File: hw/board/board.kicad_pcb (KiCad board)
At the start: 4 copper layers, 100 x 85 mm, 60 parts, among them U1 XC7A35T-FTG256, U2 TPS54331DR, U3 AP7361C-18SP-13, U4 AP7361C-10E, U5 STM32F302CBTx, U6 W25Q128JVSIQTR

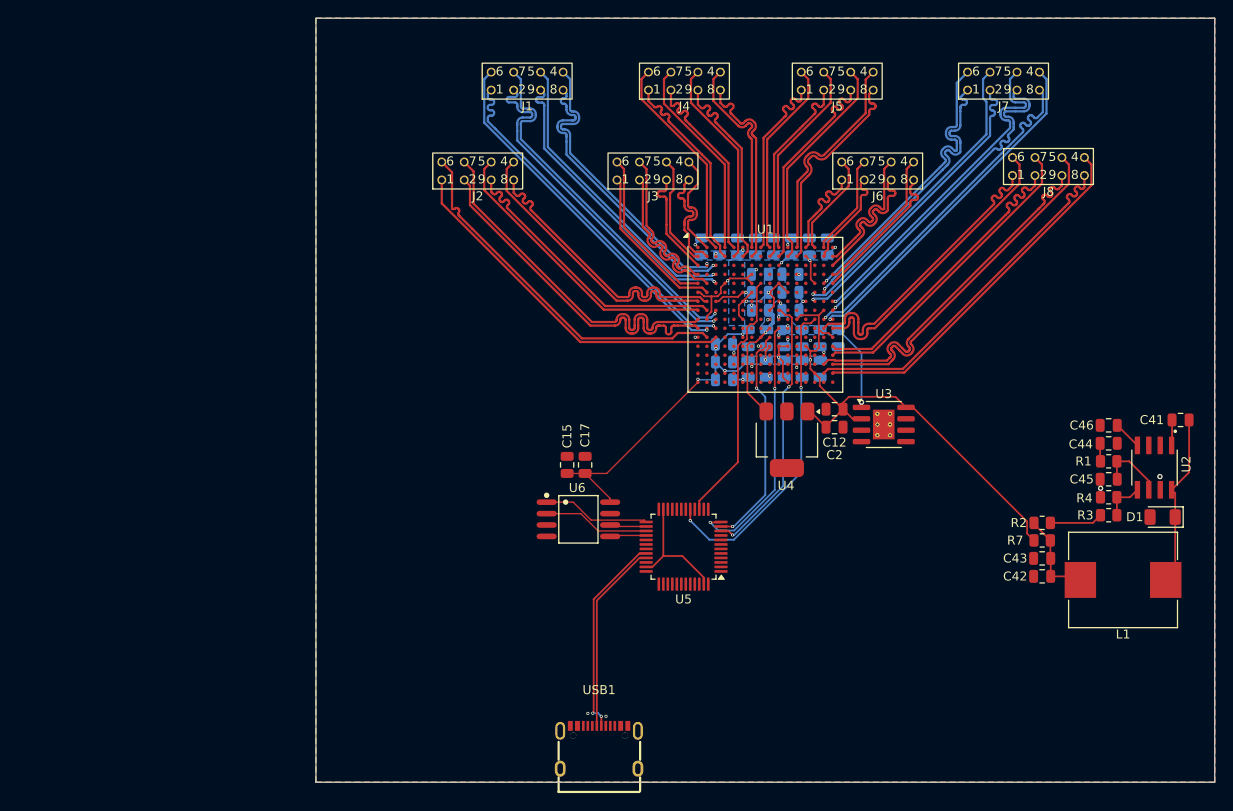
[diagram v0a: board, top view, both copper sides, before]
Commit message: Began refactoring BGA fanout
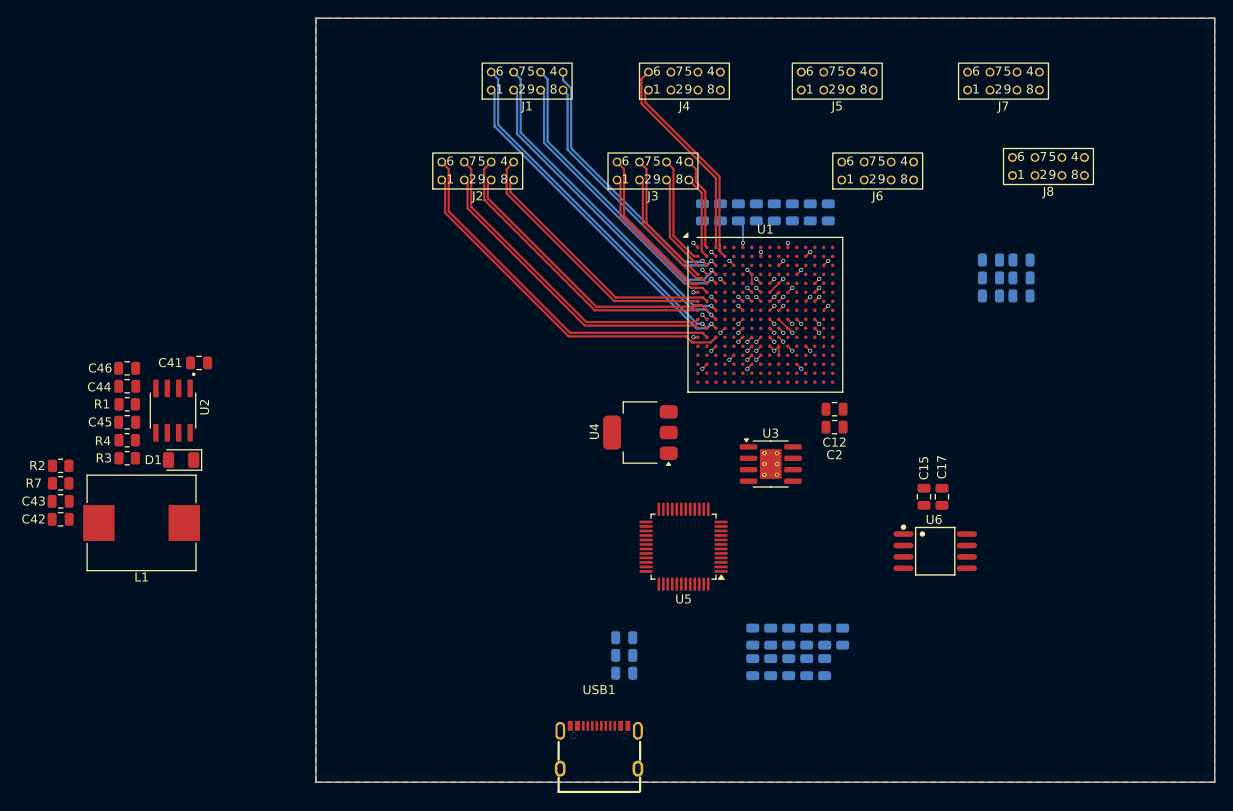
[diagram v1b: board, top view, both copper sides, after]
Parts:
- moved C44 109.4 mm to (63.0, 81.0)
- moved C45 109.4 mm to (63.0, 85.0)
- moved C42 109.4 mm to (55.6, 95.8)
- moved C43 109.4 mm to (55.6, 93.8)
- moved L1 109.4 mm to (64.6, 96.2)
- moved R2 109.4 mm to (55.6, 89.8)
- moved R7 109.4 mm to (55.6, 91.8)
- moved U2 109.4 mm to (68.1, 83.7)
- moved C41 109.4 mm to (71.0, 78.4)
- moved C46 109.4 mm to (63.0, 79.0)
- moved R1 109.4 mm to (63.0, 83.0)
- moved R3 109.4 mm to (63.0, 89.0)
- moved R4 109.4 mm to (63.0, 87.0)
- moved D1 109.4 mm to (69.0, 89.2)
- moved C15 39.9 mm to (151.7, 93.2)
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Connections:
- net VCCO_14 renamed +2V5
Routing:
- net +2V5: track 122.8 -> 17.0 mm, vias 14 -> 17
- net S_{out}8_N: track 40.9 -> 0.00 mm
- net S_{out}8_P: track 40.8 -> 0.00 mm
- net D_{out}8_N: track 40.7 -> 0.00 mm
- net D_{out}8_P: track 40.7 -> 0.00 mm
- net S_{out}7_N: track 38.9 -> 0.00 mm, vias 1 -> 0
- net S_{out}7_P: track 38.8 -> 0.00 mm, vias 1 -> 0
- net D_{out}7_N: track 38.8 -> 0.00 mm, vias 1 -> 0
- net D_{out}7_P: track 38.7 -> 0.00 mm, vias 1 -> 0
- net DIN: track 35.7 -> 0.71 mm, vias 2 -> 1
- net S_{in}8_N: track 34.4 -> 0.00 mm
- net D_{in}8_N: track 34.3 -> 0.00 mm
- net S_{in}8_P: track 34.3 -> 0.00 mm
- net D_{in}8_P: track 34.2 -> 0.00 mm
- net S_{in}7_N: track 34.4 -> 0.71 mm
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- removed copper zone on B.Cu, net +1V0
- removed copper zone on B.Cu, net +1V8
- removed copper zone on B.Cu, net +2V5

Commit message: Finished re-routing spacewire connectors
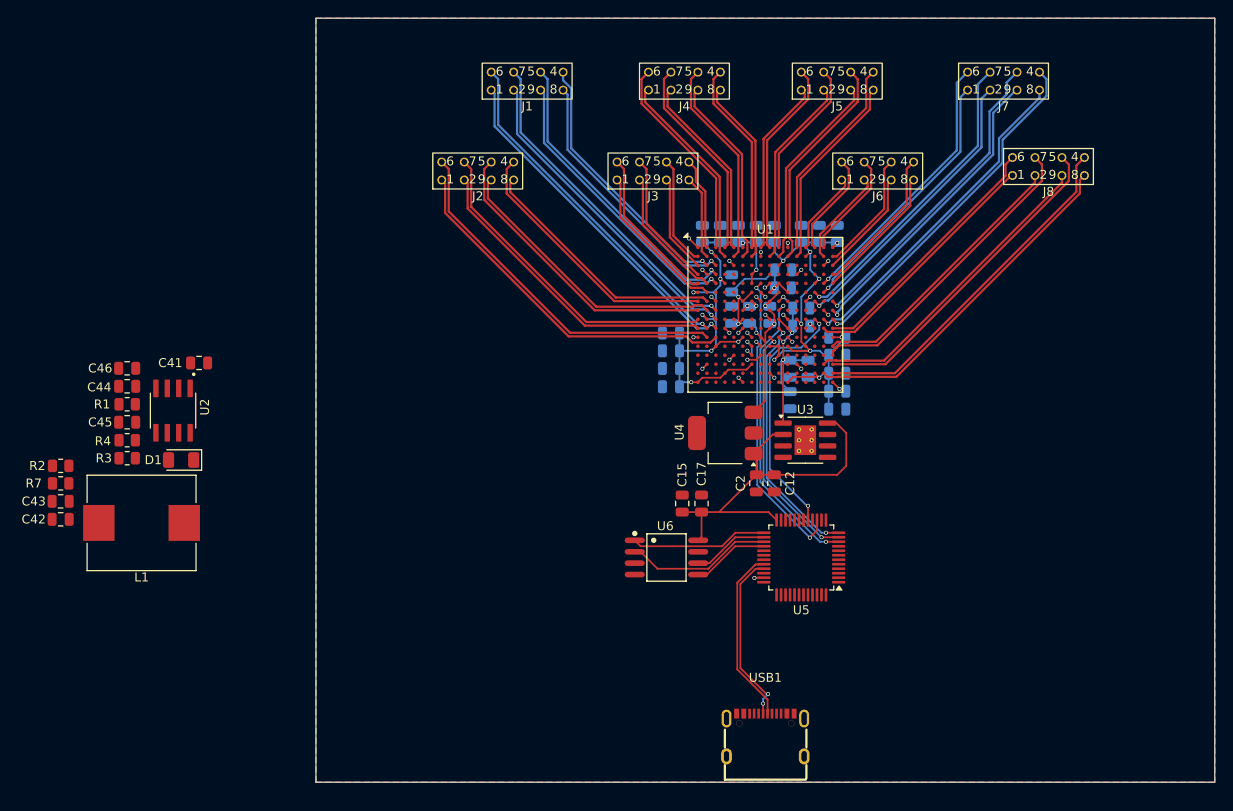
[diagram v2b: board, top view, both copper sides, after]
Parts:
- moved C8 40.8 mm to (136.0, 68.0), turned to 0 degrees
- moved C33 34.7 mm to (142.0, 77.5), turned to 0 degrees
- moved C16 34.6 mm to (142.0, 75.5), turned to 180 degrees
- moved C4 34.6 mm to (138.0, 74.2), turned to 0 degrees
- moved C35 34.3 mm to (123.5, 79.0)
- moved C37 34.3 mm to (123.5, 77.0)
- moved C36 34.3 mm to (123.5, 75.0)
- moved C32 32.9 mm to (142.0, 79.5), turned to 0 degrees
- moved C1 32.5 mm to (123.5, 81.0), turned to 180 degrees
- moved C14 32.4 mm to (130.2, 69.5), turned to 90 degrees
- moved C34 31.2 mm to (142.0, 81.5), turned to 0 degrees
- moved C9 30.0 mm to (136.8, 79.0)
- moved U6 29.9 mm to (123.0, 100.0)
- moved C3 29.9 mm to (138.8, 79.0)
- moved C31 29.6 mm to (142.0, 83.5), turned to 0 degrees
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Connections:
- U5 pad 1: unconnected-(U5-VBAT-Pad1) -> +2V5
- U5 pad 23: Net-(U5-VSS-Pad23) -> GND
- U5 pad 24: unconnected-(U5-VDD-Pad24) -> +2V5
- U5 pad 35: Net-(U5-VSS-Pad23) -> GND
- U5 pad 36: unconnected-(U5-VDD-Pad36) -> +2V5
- U5 pad 47: Net-(U5-VSS-Pad23) -> GND
- U5 pad 48: unconnected-(U5-VDD-Pad48) -> +2V5
- U5 pad 8: unconnected-(U5-VSSA-Pad8) -> GND
- U5 pad 9: unconnected-(U5-VDDA-Pad9) -> +2V5
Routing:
- net +2V5: track 17.0 -> 155.0 mm, vias 17 -> 19
- net S_{out}8_N: track 0.00 -> 39.6 mm
- net S_{out}8_P: track 0.00 -> 39.3 mm
- net S_{out}7_N: track 0.00 -> 39.0 mm, vias 0 -> 1
- net D_{out}8_N: track 0.00 -> 37.6 mm
- net S_{out}7_P: track 0.00 -> 37.0 mm, vias 0 -> 1
- net D_{out}8_P: track 0.00 -> 35.7 mm
- net D_{out}7_N: track 0.00 -> 35.0 mm, vias 0 -> 1
- net S_{in}8_N: track 0.00 -> 34.5 mm
- net D_{out}7_P: track 0.00 -> 34.1 mm, vias 0 -> 1
- net S_{in}7_N: track 0.71 -> 34.1 mm
- net CCLK: track 0.71 -> 33.6 mm, vias 1 -> 2
- net DONE: track 0.71 -> 32.8 mm, vias 1 -> 2
- net S_{in}7_P: track 0.71 -> 32.8 mm
- net S_{in}8_P: track 0.00 -> 30.8 mm
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
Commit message: Added reset + boot switches for STM32, re-routed power
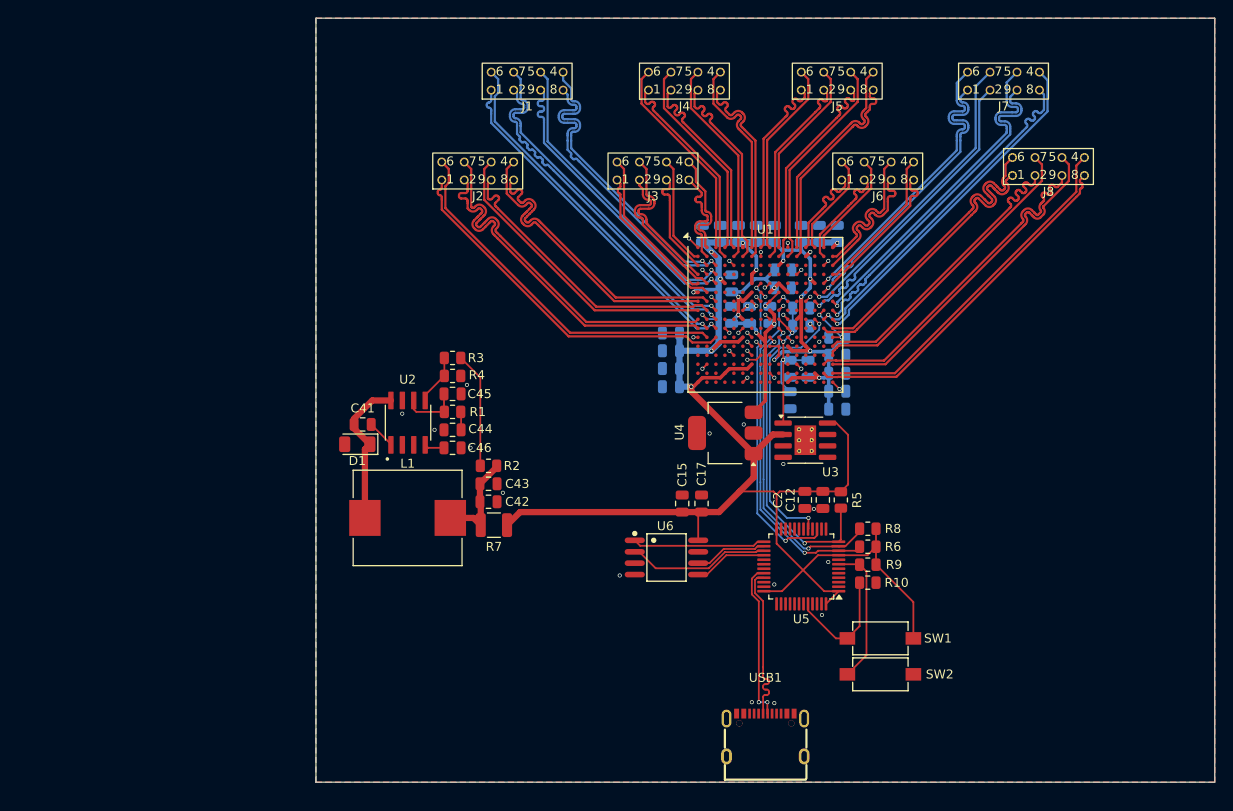
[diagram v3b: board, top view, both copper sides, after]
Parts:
- added R10: 4k7, Resistor_SMD:R_0805_2012Metric, F.Cu at (145.4, 102.8)
- added R5: 4k7, Resistor_SMD:R_0805_2012Metric, F.Cu at (142.4, 93.6)
- added R6: 330, Resistor_SMD:R_0805_2012Metric, F.Cu at (145.4, 98.8)
- added R8: 4k7, Resistor_SMD:R_0805_2012Metric, F.Cu at (145.4, 96.8)
- added R9: 4k7, Resistor_SMD:R_0805_2012Metric, F.Cu at (145.4, 100.8)
- added SW1: TSB008A2526A, EasyEDA:SW-SMD_L6.0-W3.5-LS8.0, F.Cu at (146.8, 109.0)
- added SW2: TSB008A2526A, EasyEDA:SW-SMD_L6.0-W3.5-LS8.0, F.Cu at (146.8, 113.0)
- R7: footprint Resistor_SMD:R_0805_2012Metric -> Resistor_SMD:R_1210_3225Metric
- moved R7 48.4 mm to (103.8, 96.4), turned to 0 degrees
- moved C43 47.6 mm to (103.2, 91.8), turned to 0 degrees
- moved C42 47.6 mm to (103.2, 93.8), turned to 0 degrees
- moved R2 47.6 mm to (103.2, 89.8), turned to 180 degrees
- moved R3 37.9 mm to (99.2, 77.8), turned to 180 degrees
- moved C46 37.3 mm to (99.2, 87.8), turned to 0 degrees
- moved R4 36.9 mm to (99.2, 79.8), turned to 0 degrees
- moved C44 36.5 mm to (99.2, 85.8), turned to 180 degrees
- moved C45 36.3 mm to (99.2, 81.8), turned to 0 degrees
- moved R1 36.2 mm to (99.2, 83.8), turned to 0 degrees
- moved L1 29.6 mm to (94.2, 95.6), turned to 0 degrees
- moved U2 26.2 mm to (94.2, 85.0), turned to 90 degrees
- moved D1 19.7 mm to (88.6, 87.4)
- moved C41 19.4 mm to (89.2, 85.2), turned to 0 degrees
- moved C12 5.71 mm to (140.4, 93.6)
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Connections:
- U5 pad 44: unconnected-(U5-BOOT0-Pad44) -> Net-(U5-BOOT0)
- U5 pad 7: unconnected-(U5-NRST-Pad7) -> Net-(U5-NRST)
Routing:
- net +2V5: track 155.0 -> 235.7 mm, vias 19 -> 18
- net Net-(D1-K): track 0.00 -> 16.9 mm
- net Net-(U5-NRST): track 0.00 -> 15.7 mm
- net Net-(U5-BOOT0): track 0.00 -> 13.2 mm
- net Net-(R2-Pad2): track 0.00 -> 12.9 mm
- net Net-(C42-Pad1): track 0.00 -> 11.1 mm
- net Net-(U2-COMP): track 0.00 -> 6.52 mm
- net INIT_B: track 28.2 -> 34.3 mm
- net S_{in}2_P: track 34.5 -> 40.5 mm
- net PROGRAM_B: track 27.7 -> 33.6 mm
- net D_{in}8_P: track 28.4 -> 34.1 mm
- net D_{in}8_N: track 28.6 -> 34.3 mm
- net Net-(U2-VSENSE): track 0.00 -> 5.61 mm
- net DONE: track 32.8 -> 37.7 mm
- net S_{out}2_P: track 28.4 -> 33.2 mm
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
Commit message: Added power connector, SWD/JTAG connectors
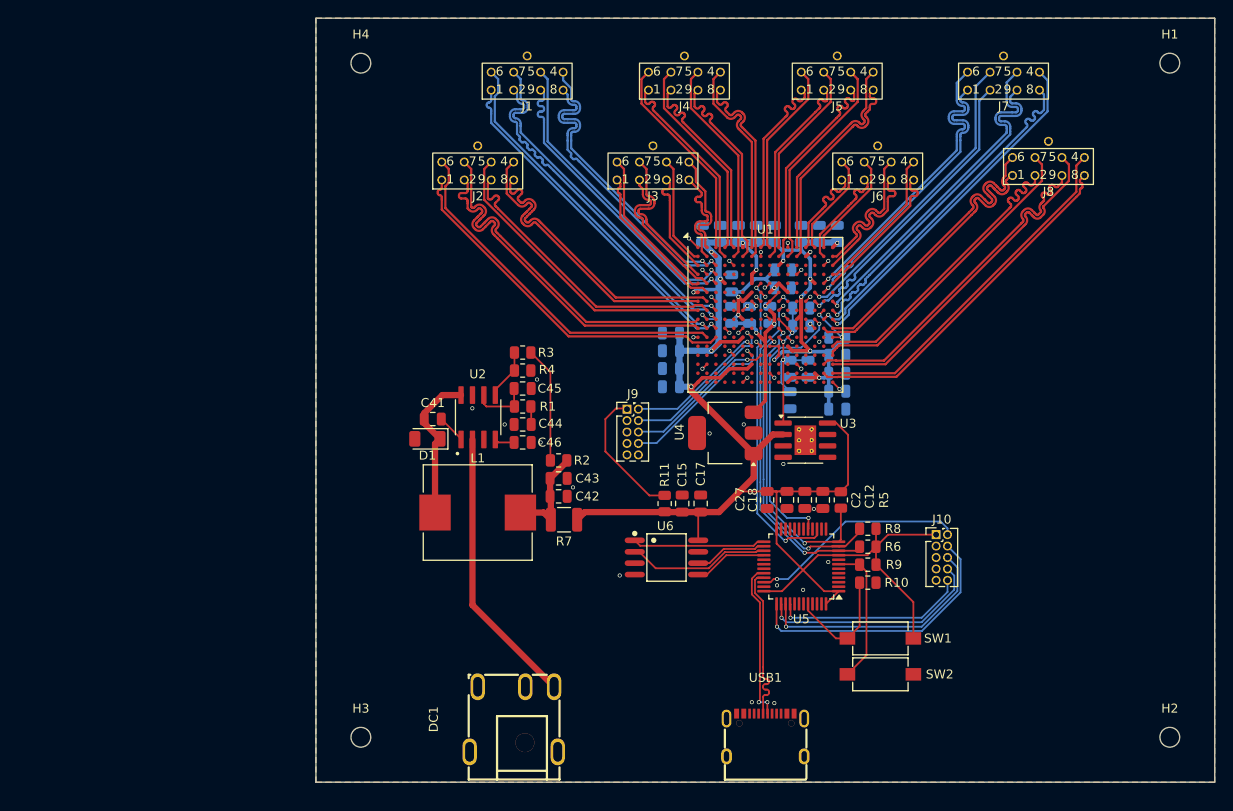
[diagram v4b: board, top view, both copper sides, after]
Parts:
- added C18: 47u, Capacitor_SMD:C_0805_2012Metric, F.Cu at (136.4, 93.6)
- added C27: 470n, Capacitor_SMD:C_0805_2012Metric, F.Cu at (134.2, 93.6)
- added DC1: DC-044A-20A, EasyEDA:DC-IN-TH_DC-044A-20A, F.Cu at (106.0, 118.0)
- added H1: MountingHole, MountingHole:MountingHole_2.2mm_M2, F.Cu at (179.0, 45.0)
- added H2: MountingHole, MountingHole:MountingHole_2.2mm_M2, F.Cu at (179.0, 120.0)
- added H3: MountingHole, MountingHole:MountingHole_2.2mm_M2, F.Cu at (89.0, 120.0)
- added H4: MountingHole, MountingHole:MountingHole_2.2mm_M2, F.Cu at (89.0, 45.0)
- added J10: Conn_ARM_JTAG_SWD_10, Connector_PinHeader_1.27mm:PinHeader_2x05_P1.27mm_Vertical, F.Cu at (153.0, 97.5)
- added J9: Conn_ARM_JTAG_SWD_10, Connector_PinHeader_1.27mm:PinHeader_2x05_P1.27mm_Vertical, F.Cu at (118.6, 83.5)
- added R11: 0, Resistor_SMD:R_0805_2012Metric, F.Cu at (122.8, 94.0)
- moved D1 7.82 mm to (96.4, 86.8)
- moved C41 7.82 mm to (97.0, 84.6)
- moved C42 7.82 mm to (111.0, 93.2)
- moved C43 7.82 mm to (111.0, 91.2)
- moved C44 7.82 mm to (107.0, 85.2)
- moved C45 7.82 mm to (107.0, 81.2)
- moved C46 7.82 mm to (107.0, 87.2)
- moved L1 7.82 mm to (102.0, 95.0)
- moved R1 7.82 mm to (107.0, 83.2)
- moved R2 7.82 mm to (111.0, 89.2)
- moved R3 7.82 mm to (107.0, 77.2)
- moved R4 7.82 mm to (107.0, 79.2)
- moved R7 7.82 mm to (111.6, 95.8)
- moved U2 7.82 mm to (102.0, 84.4)
- moved C17 0.10 mm to (126.8, 94.0)
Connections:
- U2 pad 2: +12V -> Net-(U2-VIN)
- U5 pad 34: unconnected-(U5-PA13-Pad34) -> SWDIO
- U5 pad 37: unconnected-(U5-PA14-Pad37) -> SWCLK
- U5 pad 38: unconnected-(U5-PA15-Pad38) -> JTDI
- U5 pad 39: unconnected-(U5-PB3-Pad39) -> JTDO
- U5 pad 40: unconnected-(U5-PB4-Pad40) -> ~{JTRST}
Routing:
- net Net-(U2-VIN): track 0.00 -> 31.3 mm
- net SWCLK: track 0.00 -> 30.7 mm, vias 0 -> 1
- net JTDO: track 0.00 -> 27.5 mm, vias 0 -> 1
- net JTDI: track 0.00 -> 25.1 mm, vias 0 -> 1
- net SWDIO: track 0.00 -> 24.2 mm, vias 0 -> 1
- net ~{JTRST}: track 0.00 -> 21.5 mm, vias 0 -> 1
- net TDI: track 0.71 -> 18.4 mm
- net TCK: track 0.71 -> 18.1 mm
- net TDO: track 1.71 -> 17.0 mm
- net TMS: track 0.71 -> 15.8 mm
- net Net-(J9-VTref): track 0.00 -> 15.0 mm
- net +2V5: track 235.7 -> 236.7 mm

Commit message: Reannotated piece numbers
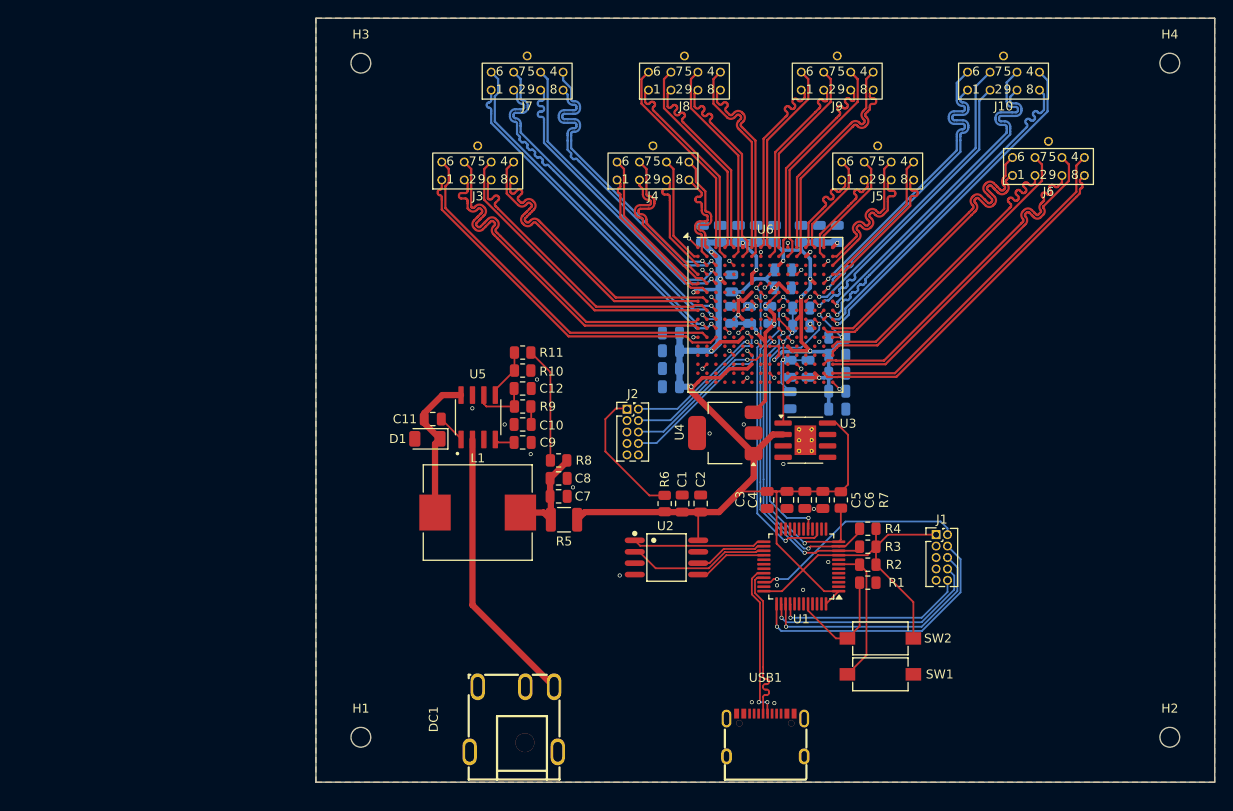
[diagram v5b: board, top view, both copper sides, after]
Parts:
- renumbered C15 to C1, C44 to C10, C41 to C11, C45 to C12, C31 to C13, C7 to C14, C34 to C15, C1 to C16, C32 to C17, C3 to C18, C9 to C19, C17 to C2, C35 to C20, C33 to C21, C37 to C22, C16 to C23, C36 to C24, C4 to C25, C11 to C26, C13 to C27, C10 to C28, C5 to C29, C27 to C3, C6 to C30, C14 to C31, C8 to C32, C21 to C33, C19 to C34, C22 to C35, C20 to C36, C24 to C37, C26 to C38, C25 to C39, C18 to C4, C23 to C40, C2 to C5, C12 to C6, C42 to C7, C43 to C8, C46 to C9, H3 to H1, H4 to H3, H1 to H4, J10 to J1, J7 to J10, J9 to J2, J2 to J3, J3 to J4, J6 to J5, J8 to J6, J1 to J7, J4 to J8, J5 to J9, R10 to R1, R4 to R10, R3 to R11, R9 to R2, R6 to R3, R8 to R4, R7 to R5, R11 to R6, R5 to R7, R2 to R8, R1 to R9, SW2 to SW1, SW1 to SW2, U5 to U1, U6 to U2, U2 to U5, U1 to U6
